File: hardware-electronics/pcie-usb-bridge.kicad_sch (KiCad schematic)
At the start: 64 parts, among them U10 24AA04T-I_OT, U3 PI7C9X440SLBFDE, Y1 ABM8-12.000MHZ-B2-T

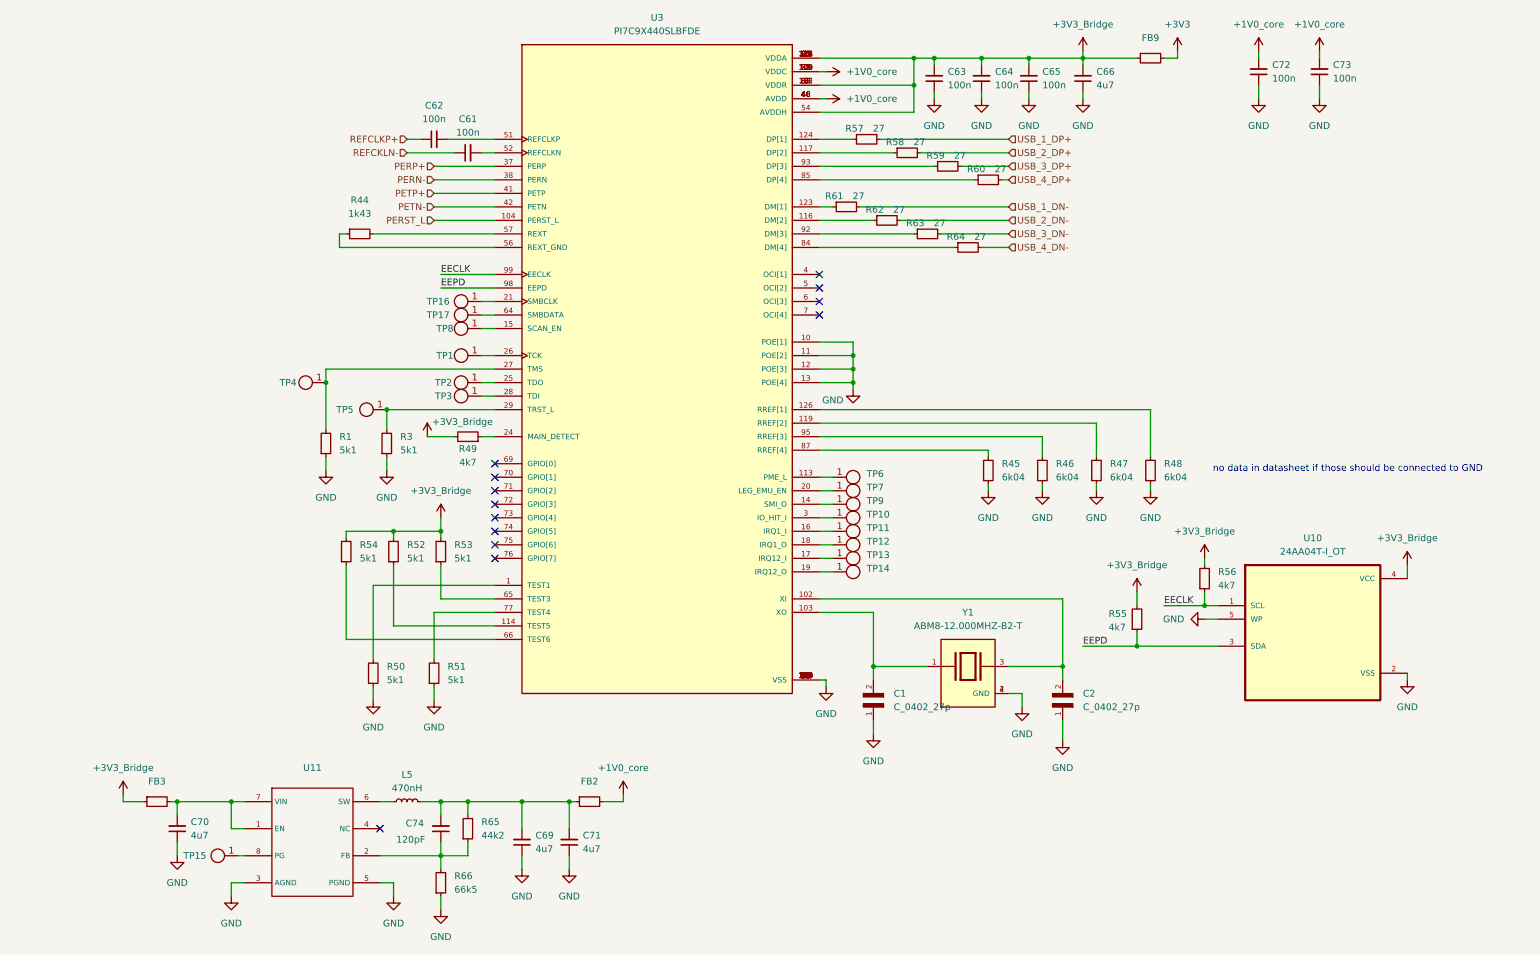
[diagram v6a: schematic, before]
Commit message: [#16] 1V0 DCDC add cap after FB
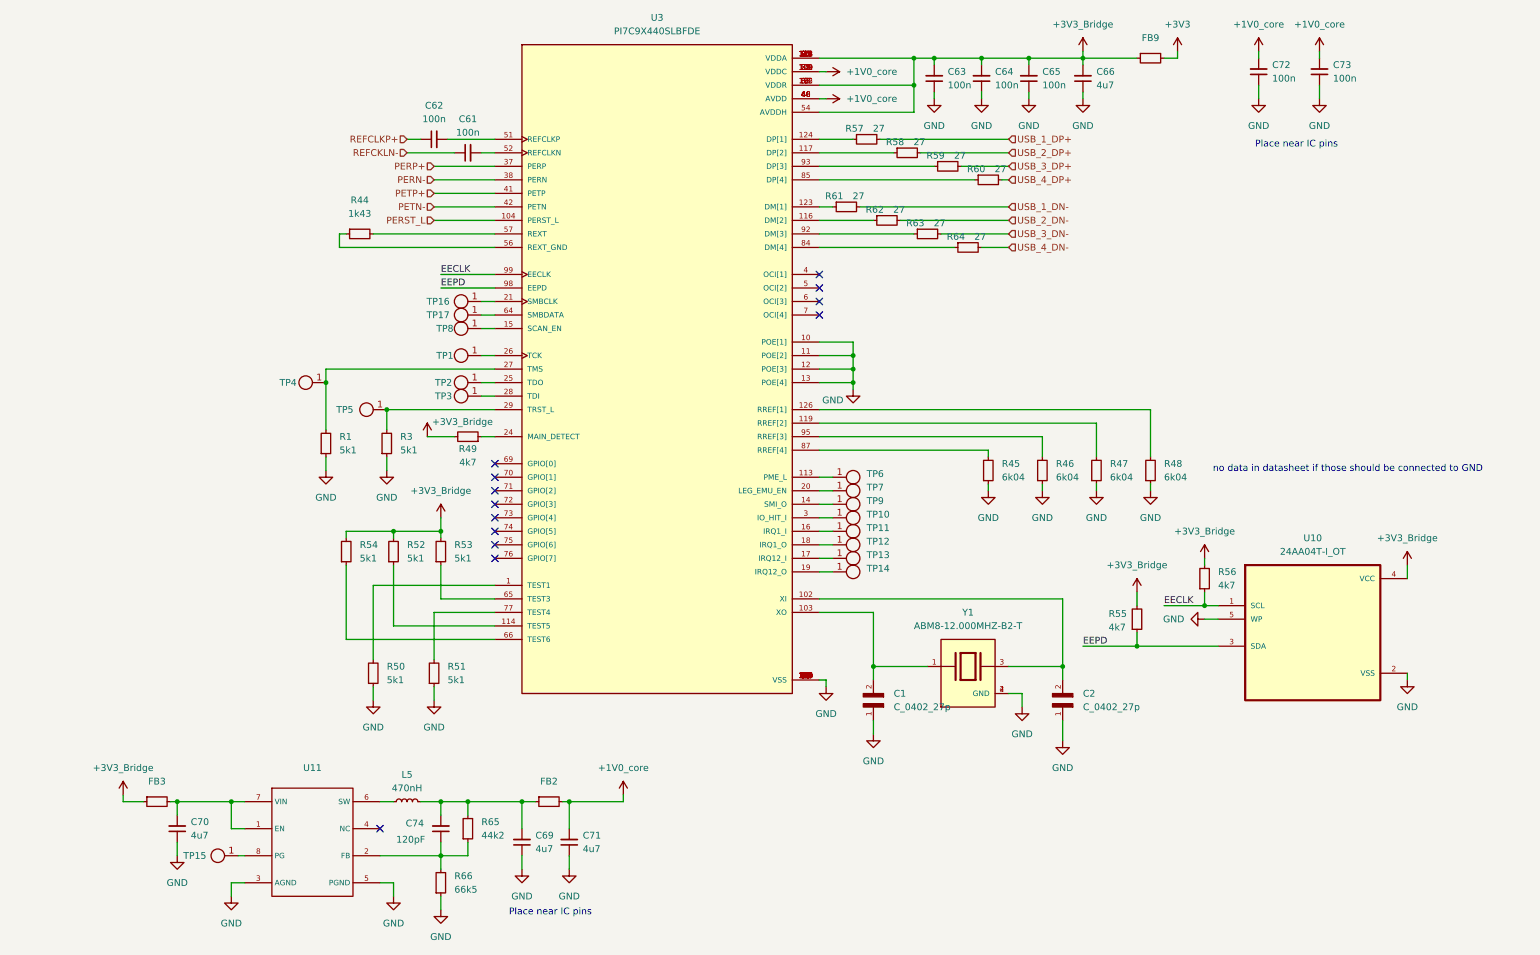
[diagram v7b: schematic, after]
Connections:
- net +1V0_core: now also C71.2
- net at C69.2, C74.2, FB2.1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: no longer C71.2
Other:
- note added: "Place near IC pins"
- moved on the sheet: FB2
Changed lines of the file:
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@@
 	)
 	(junction
-		(at 101.6 166.37)
+		(at 173.99 87.63)
 		(diameter 0)
 		(color 0 0 0 0)
 	)
 	(junction
-		(at 173.99 87.63)
+		(at 57.15 166.37)
 		(diameter 0)
 		(color 0 0 0 0)
 	)
 	(junction
-		(at 57.15 166.37)
+		(at 46.99 166.37)
 		(diameter 0)
 		(color 0 0 0 0)
 	)
 	(junction
-		(at 46.99 166.37)
+		(at 101.6 166.37)
 		(diameter 0)
 		(color 0 0 0 0)
@@
 	)
 	(junction
-		(at 96.52 176.53)
+		(at 111.76 166.37)
 		(diameter 0)
 		(color 0 0 0 0)
 	)
 	(junction
-		(at 74.93 87.63)
+		(at 96.52 176.53)
 		(diameter 0)
 		(color 0 0 0 0)
 	)
 	(junction
-		(at 173.99 82.55)
+		(at 74.93 87.63)
 		(diameter 0)
 		(color 0 0 0 0)
 	)
 	(junction
-		(at 111.76 166.37)
+		(at 173.99 82.55)
 		(diameter 0)
 		(color 0 0 0 0)
@@
 	)
 	(junction
-		(at 120.65 166.37)
-		(diameter 0)
-		(color 0 0 0 0)
-	)
-	(junction
 		(at 207.01 26.67)
 		(diameter 0)
@@
 	)
 	(junction
+		(at 120.65 166.37)
+		(diameter 0)
+		(color 0 0 0 0)
+	)
+	(junction
 		(at 86.36 92.71)
 		(diameter 0)
@@
 	(wire
 		(pts
+			(xy 101.6 166.37) (xy 111.76 166.37)
+		)
+		(stroke
+			(width 0)
+			(type default)
+		)
+	)
+	(wire
+		(pts
 			(xy 106.68 130.81) (xy 95.25 130.81)
 		)
@@
 	(wire
 		(pts
-			(xy 101.6 166.37) (xy 111.76 166.37)
-		)
-		(stroke
-			(width 0)
-			(type default)
-		)
-	)
-	(wire
-		(pts
 			(xy 190.5 59.69) (xy 203.2 59.69)
 		)
@@
 	(wire
 		(pts
+			(xy 119.38 166.37) (xy 120.65 166.37)
+		)
+		(stroke
+			(width 0)
+			(type default)
+		)
+	)
+	(wire
+		(pts
 			(xy 173.99 82.55) (xy 167.64 82.55)
 		)
@@
 	(wire
 		(pts
-			(xy 120.65 166.37) (xy 121.92 166.37)
+			(xy 120.65 166.37) (xy 130.81 166.37)
 		)
 		(stroke
@@
 	(wire
 		(pts
+			(xy 111.76 166.37) (xy 114.3 166.37)
+		)
+		(stroke
+			(width 0)
+			(type default)
+		)
+	)
+	(wire
+		(pts
 			(xy 99.06 97.79) (xy 93.98 97.79)
 		)
@@
 	(wire
 		(pts
-			(xy 120.65 166.37) (xy 111.76 166.37)
-		)
-		(stroke
-			(width 0)
-			(type default)
-		)
-	)
-	(wire
-		(pts
 			(xy 185.42 26.67) (xy 189.23 26.67)
 		)
@@
 	(wire
 		(pts
-			(xy 127 166.37) (xy 130.81 166.37)
-		)
-		(stroke
-			(width 0)
-			(type default)
-		)
-	)
-	(wire
-		(pts
 			(xy 106.68 125.73) (xy 83.82 125.73)
 		)
@@
 		)
 	)
+	(text "Place near IC pins\n"
+		(exclude_from_sim no)
+		(at 257.302 42.926 0)
+		(effects
+			(font
+				(size 1.27 1.27)
+			)
+		)
+	)
+	(text "Place near IC pins\n"
+		(exclude_from_sim no)
+		(at 117.094 187.198 0)
+		(effects
+			(font
+				(size 1.27 1.27)
+			)
+		)
+	)
 	(label "EECLK"
 		(at 96.52 67.31 0)
@@
 	(symbol
 		(lib_id "M2SmartHomeSymbols:FB_120R_0603")
-		(at 121.92 166.37 0)
+		(at 114.3 166.37 0)
 		(unit 1)
 		(exclude_from_sim no)
@@
 		(fields_autoplaced yes)
 		(property "Reference" "FB2"
-			(at 124.46 162.56 0)
+			(at 116.84 162.56 0)
 			(effects
 				(font
@@
 		)
 		(property "Value" "FB_120R_0603"
-			(at 142.24 176.53 0)
+			(at 134.62 176.53 0)
 			(effects
 				(font
@@
 		)
 		(property "Footprint" "M2SmartHomeFootprints:FB_0603"
-			(at 142.24 179.07 0)
+			(at 134.62 179.07 0)
 			(effects
 				(font
@@
 		)
 		(property "Datasheet" "https://www.murata.com/products/productdetail?partno=BLM18AG121SN1D"
-			(at 142.24 181.61 0)
+			(at 134.62 181.61 0)
 			(effects
 				(font
@@
 		)
 		(property "Description" "SMD Ferrite Bead, 120 Ω @ 100 MHz, 2 A, 0603 [1608 Metric], BLM18A Series"
-			(at 121.92 166.37 0)
+			(at 114.3 166.37 0)
 			(effects
 				(font
@@
 		)
 		(property "MPN" "BLM18AG121SN1D"
-			(at 142.24 184.15 0)
+			(at 134.62 184.15 0)
 			(effects
 				(font
@@
 		)
 		(property "Manufacturer" "Murata"
-			(at 142.24 186.69 0)
+			(at 134.62 186.69 0)
 			(effects
 				(font
@@
 		)
 		(property "License" "Apache-2.0"
-			(at 142.24 189.23 0)
+			(at 134.62 189.23 0)
 			(effects
 				(font
@@
 		)
 		(property "Author" "Your Name"
-			(at 142.24 191.77 0)
+			(at 134.62 191.77 0)
 			(effects
 				(font
@@
 		)
 		(property "Impedance" "120R @ 100 MHz"
-			(at 142.24 194.31 0)
+			(at 134.62 194.31 0)
 			(effects
 				(font
@@
 		)
 		(property "Current" "2A"
-			(at 142.24 196.85 0)
+			(at 134.62 196.85 0)
 			(effects
 				(font

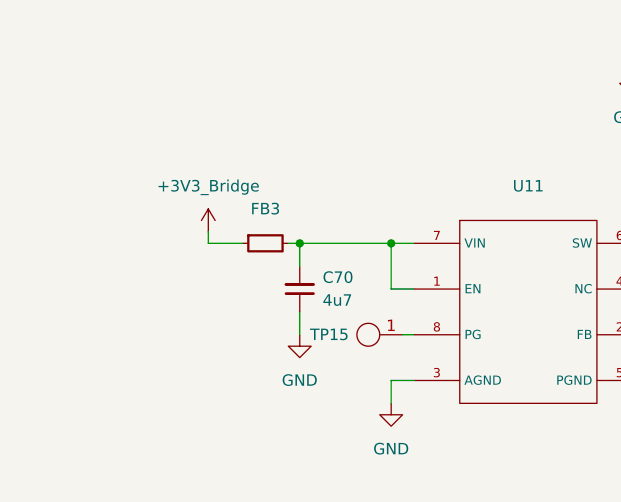
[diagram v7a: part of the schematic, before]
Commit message: [#16] 1V0 DCDC add pull up for PG
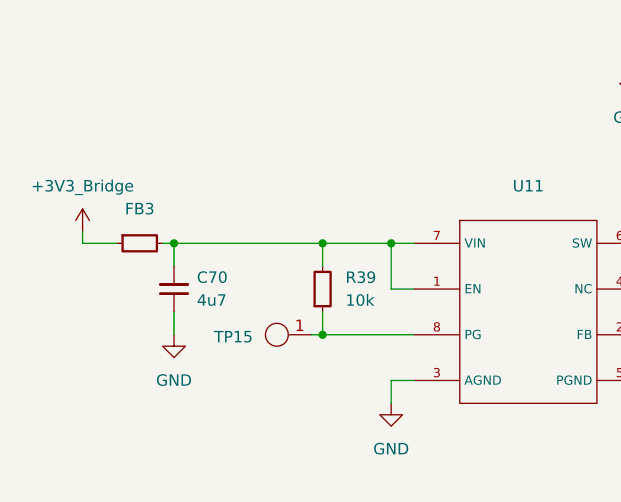
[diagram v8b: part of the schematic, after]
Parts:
- added R39: R_10k_0402, M2SmartHomeFootprints:R_0402, symbol M2SmartHomeSymbols:R_10k_0402
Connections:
- net at C70.2, FB3.2, U11.1 (EN)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: now also R39.2
- net at TP15.1, U11.8 (PG): now also R39.1
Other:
- moved on the sheet: C70, FB3, TP15
